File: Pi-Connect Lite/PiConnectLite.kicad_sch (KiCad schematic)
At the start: 53 parts, among them J1 40HAT, J2 Conn_01x02, J3 Ext_Switch, J4 Conn_Telemetry, J5 Conn_01x02, J6 Power_Pad, J7 Conn_Telemetry, Q1 DMMT5401, Q2 SI2323, SW1 SW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

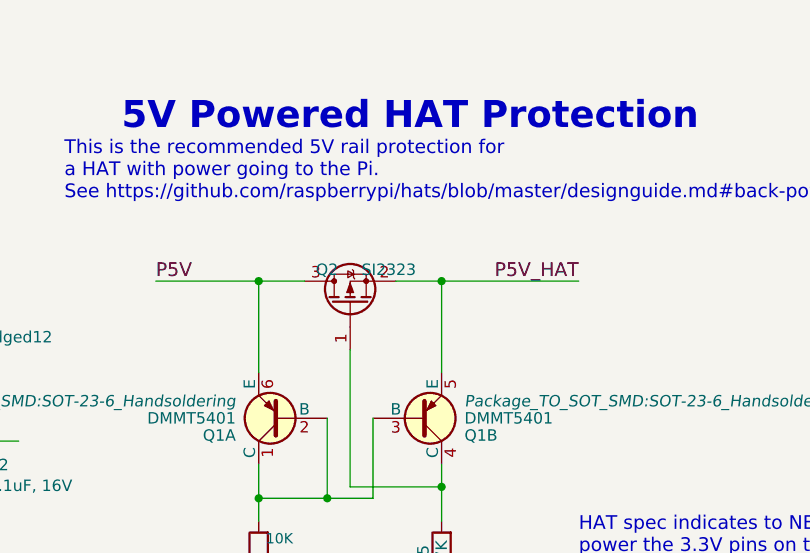
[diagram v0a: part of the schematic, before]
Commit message: Add TSM2323 as Q1
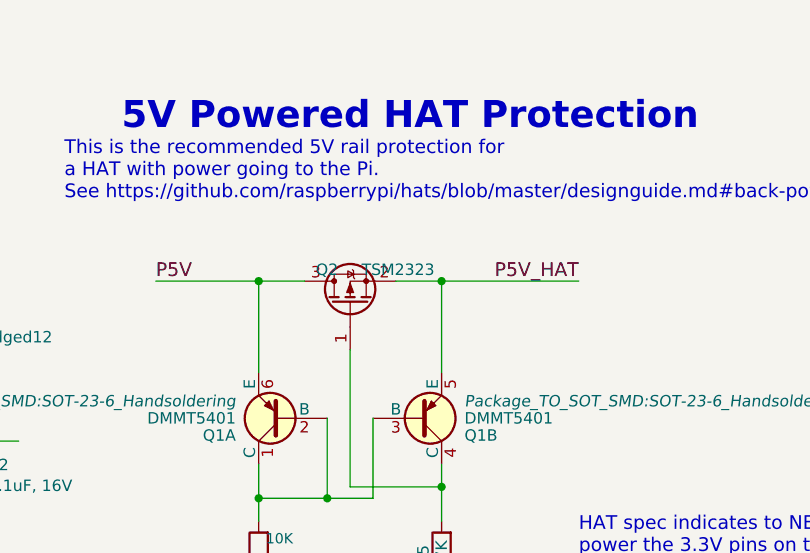
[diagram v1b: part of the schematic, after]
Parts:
- Q2: value SI2323 -> TSM2323; MFR Vishay Siliconix -> Taiwan Semiconductor Corporation; MPN SI2323DDS-T1-GE3 -> TSM2323CX RFG; SPN SI2323DDS-T1-GE3CT-ND -> 1801-TSM2323CXRFGCT-ND
- U6: footprint Silicon-Standard:SC70 -> Package_TO_SOT_SMD:SOT-353_SC-70-5
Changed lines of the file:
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@@
       (effects (font (size 1.27 1.27)) (justify right))
     )
-    (property "Value" "SI2323" (id 1) (at 157.48 59.69 90)
+    (property "Value" "TSM2323" (id 1) (at 157.48 59.69 90)
       (effects (font (size 1.27 1.27)) (justify right))
     )
@@
     )
     (property "Datasheet" "" (id 3) (at 156.21 63.5 0))
-    (property "MFR" "Vishay Siliconix" (id 4) (at 217.17 219.71 0)
-      (effects (font (size 1.27 1.27)) hide)
-    )
-    (property "MPN" "SI2323DDS-T1-GE3" (id 5) (at 217.17 219.71 0)
-      (effects (font (size 1.27 1.27)) hide)
-    )
-    (property "SPN" "SI2323DDS-T1-GE3CT-ND" (id 6) (at 217.17 219.71 0)
+    (property "MFR" "Taiwan Semiconductor Corporation" (id 4) (at 217.17 219.71 0)
+      (effects (font (size 1.27 1.27)) hide)
+    )
+    (property "MPN" "TSM2323CX RFG" (id 5) (at 217.17 219.71 0)
+      (effects (font (size 1.27 1.27)) hide)
+    )
+    (property "SPN" "1801-TSM2323CXRFGCT-ND" (id 6) (at 217.17 219.71 0)
       (effects (font (size 1.27 1.27)) hide)
     )
@@
     (pin "2")
     (pin "6")
-  )
-  (symbol (lib_id "PiBits:DMMT5401") (at 163.83 76.2 0) (mirror x) (unit 2)
-    (in_bom yes) (on_board yes)
-    (property "Reference" "Q1" (id 0) (at 168.91 78.105 0)
-      (effects (font (size 1.27 1.27)) (justify left))
-    )
-    (property "Value" "DMMT5401" (id 1) (at 168.91 76.2 0)
-      (effects (font (size 1.27 1.27)) (justify left))
-    )
-    (property "Footprint" "Package_TO_SOT_SMD:SOT-23-6_Handsoldering" (id 2) (at 168.91 74.295 0)
-      (effects (font (size 1.27 1.27) italic) (justify left))
-    )
-    (property "Datasheet" "" (id 3) (at 163.83 76.2 0)
-      (effects (font (size 1.27 1.27)) (justify left))
-    )
-    (property "MFR" "DiodesZetex" (id 4) (at 0 0 0)
-      (effects (font (size 1.27 1.27)) hide)
-    )
-    (property "MPN" "DMMT5401-7-F" (id 5) (at 0 0 0)
-      (effects (font (size 1.27 1.27)) hide)
-    )
-    (property "SPN" "DMMT5401-FDICT-ND" (id 6) (at 0 0 0)
-      (effects (font (size 1.27 1.27)) hide)
-    )
-    (property "SPR" "Digikey" (id 7) (at 0 0 0)
-      (effects (font (size 1.27 1.27)) hide)
-    )
-    (property "Max Temp (C)" "150" (id 8) (at 163.83 76.2 0)
-      (effects (font (size 1.27 1.27)) hide)
-    )
-    (property "Min Temp (C)" "-55" (id 9) (at 163.83 76.2 0)
-      (effects (font (size 1.27 1.27)) hide)
-    )
     (pin "3")
     (pin "4")
     (pin "5")
   )
+  (symbol (lib_id "PiBits:DMMT5401") (at 163.83 76.2 0) (mirror x) (unit 2)
+    (in_bom yes) (on_board yes)
+    (property "Reference" "Q1" (id 0) (at 168.91 78.105 0)
+      (effects (font (size 1.27 1.27)) (justify left))
+    )
+    (property "Value" "DMMT5401" (id 1) (at 168.91 76.2 0)
+      (effects (font (size 1.27 1.27)) (justify left))
+    )
+    (property "Footprint" "Package_TO_SOT_SMD:SOT-23-6_Handsoldering" (id 2) (at 168.91 74.295 0)
+      (effects (font (size 1.27 1.27) italic) (justify left))
+    )
+    (property "Datasheet" "" (id 3) (at 163.83 76.2 0)
+      (effects (font (size 1.27 1.27)) (justify left))
+    )
+    (property "MFR" "DiodesZetex" (id 4) (at 0 0 0)
+      (effects (font (size 1.27 1.27)) hide)
+    )
+    (property "MPN" "DMMT5401-7-F" (id 5) (at 0 0 0)
+      (effects (font (size 1.27 1.27)) hide)
+    )
+    (property "SPN" "DMMT5401-FDICT-ND" (id 6) (at 0 0 0)
+      (effects (font (size 1.27 1.27)) hide)
+    )
+    (property "SPR" "Digikey" (id 7) (at 0 0 0)
+      (effects (font (size 1.27 1.27)) hide)
+    )
+    (property "Max Temp (C)" "150" (id 8) (at 163.83 76.2 0)
+      (effects (font (size 1.27 1.27)) hide)
+    )
+    (property "Min Temp (C)" "-55" (id 9) (at 163.83 76.2 0)
+      (effects (font (size 1.27 1.27)) hide)
+    )
+    (pin "1")
+    (pin "2")
+    (pin "6")
+    (pin "3")
+    (pin "4")
+    (pin "5")
+  )
   (symbol (lib_id "Device:R") (at 146.05 91.44 180) (unit 1)
     (in_bom yes) (on_board yes)
@@
     (property "Reference" "U6" (id 0) (at 348.615 108.7882 0))
     (property "Value" "NC7SZ00P5X" (id 1) (at 348.615 111.0996 0))
-    (property "Footprint" "Silicon-Standard:SC70" (id 2) (at 349.25 115.57 0)
+    (property "Footprint" "Package_TO_SOT_SMD:SOT-353_SC-70-5" (id 2) (at 349.25 115.57 0)
       (effects (font (size 1.27 1.27)) hide)
     )
@@
     )
     (path "/00000000-0000-0000-0000-000058e14eb1"
-      (reference "Q2") (unit 1) (value "SI2323") (footprint "Package_TO_SOT_SMD:SOT-23")
+      (reference "Q2") (unit 1) (value "TSM2323") (footprint "Package_TO_SOT_SMD:SOT-23")
     )
     (path "/00000000-0000-0000-0000-000058e17715"
@@
     )
     (path "/00000000-0000-0000-0000-00005c2c8597"
-      (reference "U6") (unit 1) (value "NC7SZ00P5X") (footprint "Silicon-Standard:SC70")
-    )
-  )
+      (reference "U6") (unit 1) (value "NC7SZ00P5X") (footprint "Package_TO_SOT_SMD:SOT-353_SC-70-5")
+    )
+  )

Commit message: Opensourcing
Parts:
- added SW?: SW_Push, symbol Switch:SW_Push
- added U?: STM6601CA2BDM6F, Package_DFN_QFN:TDFN-12_2x3mm_P0.5mm, symbol Power_Management:STM6601
- J1: MFR Sullins Connector Solutions -> Samtec Inc.; MPN PPPC202LFBN-RC -> ESQ-120-23-T-D; Min Temp (C) -40 -> -55; SPN S7123-ND -> SAM9315-ND
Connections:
- net GND: now also SW?.1, U?.12 (GND)
- net P_ENABLE: now also U?.9 (~{EN}/EN)
- net VCC: now also U?.1 (Vcc)
- new net: SW?.2, U?.6 (~{PB})
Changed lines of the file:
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@@
     (stroke (width 0) (type default) (color 0 0 0 0))
   )
+  (wire (pts (xy 347.98 138.43) (xy 354.33 138.43))
+    (stroke (width 0) (type default) (color 0 0 0 0))
+  )
   (wire (pts (xy 124.46 227.33) (xy 148.59 227.33))
     (stroke (width 0) (type default) (color 0 0 0 0))
@@
     (stroke (width 0) (type default) (color 0 0 0 0))
   )
+  (wire (pts (xy 384.81 140.97) (xy 402.59 140.97))
+    (stroke (width 0) (type default) (color 0 0 0 0))
+  )
   (wire (pts (xy 68.58 187.96) (xy 80.01 187.96))
     (stroke (width 0) (type default) (color 0 0 0 0))
@@
     (stroke (width 0) (type default) (color 0 0 0 0))
   )
+  (wire (pts (xy 337.82 138.43) (xy 335.28 138.43))
+    (stroke (width 0) (type default) (color 0 0 0 0))
+  )
   (wire (pts (xy 349.25 83.82) (xy 337.82 83.82))
     (stroke (width 0) (type default) (color 0 0 0 0))
@@
     (stroke (width 0) (type default) (color 0 0 0 0))
   )
+  (wire (pts (xy 358.14 128.27) (xy 369.57 128.27))
+    (stroke (width 0) (type default) (color 0 0 0 0))
+  )
   (wire (pts (xy 215.9 151.13) (xy 213.36 151.13))
     (stroke (width 0) (type default) (color 0 0 0 0))
@@
     (stroke (width 0) (type default) (color 0 0 0 0))
   )
+  (wire (pts (xy 335.28 138.43) (xy 335.28 140.97))
+    (stroke (width 0) (type default) (color 0 0 0 0))
+  )
   (wire (pts (xy 91.44 66.04) (xy 87.63 66.04))
     (stroke (width 0) (type default) (color 0 0 0 0))
@@
     (effects (font (size 1.27 1.27) italic) (justify left bottom))
   )
+  (label "LDO_3V3" (at 359.41 128.27 0)
+    (effects (font (size 1.27 1.27)) (justify left bottom))
+  )
   (label "ID_SC_EEPROM_pu" (at 31.75 194.31 0)
     (effects (font (size 1.524 1.524)) (justify left bottom))
@@
     (effects (font (size 1.27 1.27)) (justify left bottom))
   )
+  (label "P_ENABLE" (at 391.16 140.97 0)
+    (effects (font (size 1.27 1.27)) (justify left bottom))
+  )
   (label "P5V_HAT" (at 53.34 45.72 0)
     (effects (font (size 1.27 1.27)) (justify left bottom))
@@
     )
     (property "Datasheet" "" (id 3) (at 49.53 78.74 0))
-    (property "MFR" "Sullins Connector Solutions" (id 4) (at 1.27 135.89 0)
+    (property "MFR" "Samtec Inc." (id 4) (at 1.27 135.89 0)
       (effects (font (size 1.27 1.27)) hide)
     )
-    (property "MPN" "PPPC202LFBN-RC" (id 5) (at 1.27 135.89 0)
+    (property "MPN" "ESQ-120-23-T-D" (id 5) (at 1.27 135.89 0)
       (effects (font (size 1.27 1.27)) hide)
     )
-    (property "SPN" "S7123-ND" (id 6) (at 1.27 135.89 0)
+    (property "SPN" "SAM9315-ND" (id 6) (at 1.27 135.89 0)
       (effects (font (size 1.27 1.27)) hide)
     )
@@
       (effects (font (size 1.27 1.27)) hide)
     )
-    (property "Min Temp (C)" "-40" (id 9) (at 67.31 78.74 0)
+    (property "Min Temp (C)" "-55" (id 9) (at 67.31 78.74 0)
       (effects (font (size 1.27 1.27)) hide)
     )
@@
     (pin "1")
   )
+  (symbol (lib_id "power:GND") (at 369.57 158.75 0) (unit 1)
+    (in_bom yes) (on_board yes)
+    (property "Reference" "#PWR?" (id 0) (at 369.57 165.1 0)
+      (effects (font (size 1.27 1.27)) hide)
+    )
+    (property "Value" "GND" (id 1) (at 369.697 163.1442 0))
+    (property "Footprint" "" (id 2) (at 369.57 158.75 0)
+      (effects (font (size 1.27 1.27)) hide)
+    )
+    (property "Datasheet" "" (id 3) (at 369.57 158.75 0)
+      (effects (font (size 1.27 1.27)) hide)
+    )
+    (pin "1")
+  )
+  (symbol (lib_id "power:GND") (at 335.28 140.97 0) (unit 1)
+    (in_bom yes) (on_board yes)
+    (property "Reference" "#PWR?" (id 0) (at 335.28 147.32 0)
+      (effects (font (size 1.27 1.27)) hide)
+    )
+    (property "Value" "GND" (id 1) (at 335.407 145.3642 0))
+    (property "Footprint" "" (id 2) (at 335.28 140.97 0)
+      (effects (font (size 1.27 1.27)) hide)
+    )
+    (property "Datasheet" "" (id 3) (at 335.28 140.97 0)
+      (effects (font (size 1.27 1.27)) hide)
+    )
+    (pin "1")
+  )
+  (symbol (lib_id "Power_Management:STM6601") (at 369.57 143.51 0) (unit 1)
+    (in_bom yes) (on_board yes) (fields_autoplaced)
+    (property "Reference" "U?" (id 0) (at 371.5894 127 0)
+      (effects (font (size 1.27 1.27)) (justify left))
+    )
+    (property "Value" "STM6601CA2BDM6F" (id 1) (at 371.5894 129.54 0)
+      (effects (font (size 1.27 1.27)) (justify left))
+    )
+    (property "Footprint" "Package_DFN_QFN:TDFN-12_2x3mm_P0.5mm" (id 2) (at 369.57 161.29 0)
+      (effects (font (size 1.27 1.27)) hide)
+    )
+    (property "Datasheet" "https://www.st.com/content/ccc/resource/technical/document/datasheet/1f/9e/3b/43/ec/04/44/71/CD00226957.pdf/files/CD00226957.pdf/jcr:content/translations/en.CD00226957.pdf" (id 3) (at 359.41 128.27 0)
+      (effects (font (size 1.27 1.27)) hide)
+    )
+    (pin "1")
+    (pin "10")
+    (pin "11")
+    (pin "12")
+    (pin "2")
+    (pin "3")
+    (pin "4")
+    (pin "5")
+    (pin "6")
+    (pin "7")
+    (pin "8")
+    (pin "9")
+  )
+  (symbol (lib_id "Switch:SW_Push") (at 342.9 138.43 0) (unit 1)
+    (in_bom yes) (on_board yes) (fields_autoplaced)
+    (property "Reference" "SW?" (id 0) (at 342.9 130.81 0))
+    (property "Value" "SW_Push" (id 1) (at 342.9 133.35 0))
+    (property "Footprint" "" (id 2) (at 342.9 133.35 0)
+      (effects (font (size 1.27 1.27)) hide)
+    )
+    (property "Datasheet" "~" (id 3) (at 342.9 133.35 0)
+      (effects (font (size 1.27 1.27)) hide)
+    )
+    (pin "1")
+    (pin "2")
+  )
   (sheet_instances
     (path "/" (page "1"))
@@
       (reference "#PWR0120") (unit 1) (value "GND") (footprint "")
     )
+    (path "/0f016a2c-1826-4a31-af71-1729c0c4e870"
+      (reference "#PWR?") (unit 1) (value "GND") (footprint "")
+    )
+    (path "/553df30c-e830-40f1-8d9a-39a369745991"
+      (reference "#PWR?") (unit 1) (value "GND") (footprint "")
+    )
     (path "/00000000-0000-0000-0000-00005d58660f"
       (reference "C1") (unit 1) (value "10uF, 50V") (footprint "Capacitor_SMD:C_1210_3225Metric")
@@
       (reference "SW1") (unit 1) (value "SW") (footprint "Button_Switch_THT:SW_CuK_OS102011MA1QN1_SPDT_Angled")
     )
+    (path "/b41ad13e-61a6-4dad-a8a7-9bb595caa281"
+      (reference "SW?") (unit 1) (value "SW_Push") (footprint "")
+    )
     (path "/00000000-0000-0000-0000-00005cbd8a4d"
       (reference "U1") (unit 1) (value "CAT24C32") (footprint "Package_SO:SOIC-8_3.9x4.9mm_P1.27mm")
@@
       (reference "U6") (unit 1) (value "NC7SZ00P5X") (footprint "Package_TO_SOT_SMD:SOT-353_SC-70-5")
     )
+    (path "/6e57fca4-b991-4a32-af4e-5e252b70b1ab"
+      (reference "U?") (unit 1) (value "STM6601CA2BDM6F") (footprint "Package_DFN_QFN:TDFN-12_2x3mm_P0.5mm")
+    )
   )
